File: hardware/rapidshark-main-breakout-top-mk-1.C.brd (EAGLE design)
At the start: 44 x 18 mm, 14 parts, among them U1 ADAFRUIT_METRO_MINIBIGHOLES

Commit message: asdlkfjaklsdfjsdlk
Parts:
- added JP1: M03JST-PTH-VERT, a_parts:JST-3-PH-VERT-PTH
- ACCEL, PUSHER: device A_butts:JST-6-PH-VERT-PTH -> a_parts:JST-6-PH-VERT-PTH
- BUTT, CLIP, DISP, TRIG: device A_butts:JST-4-PH-VERT-PTH -> a_parts:JST-4-PH-VERT-PTH
- F1: device A_butts:PTC-1206 -> a_parts:PTC-1206
- FRAME1: device A_butts:DUMMY -> a_parts:DUMMY
- R1, R2: device A_butts:R0805 -> a_parts:R0603-TIGHTER
- TVS: device A_butts:SMA-DIODE-TVS-BIDIR -> a_parts:SMA-DIODE-TVS-BIDIR
- U$2: device A_butts:COW_SMALL -> a_parts:COW_SMALL
- U$3: device A_butts:OSHWLOGO_TINY_SILKONLY -> a_parts:OSHWLOGO_TINY_SILKONLY
- U1: device A_butts:ADAFRUIT_METRO_MINI_BIGHOLES -> a_parts:ADAFRUIT_METRO_MINI_BIGHOLES
- moved R1 1.00 mm to (38.0, 11.0)
- moved R2 1.00 mm to (38.0, 7.00)
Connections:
- removed net ACCEL_A: ACCEL.1, U1.9
- removed net ACCEL_B: ACCEL.3, U1.11
- new net N$2: U1.9
- new net N$3: U1.11
- new net N$4: U1.14
- net 5V: now also ACCEL.5, DISP.2; no longer ACCEL.4, DISP.1
- net GND: now also ACCEL.6, DISP.1; no longer ACCEL.5, DISP.2, U1.26
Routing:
- net 5V: track 70.0 -> 65.1 mm
- net ACCEL_B: track 4.89 -> 0.00 mm
- net ACCEL_A: track 4.80 -> 0.00 mm
- net SDA: track 15.2 -> 13.9 mm

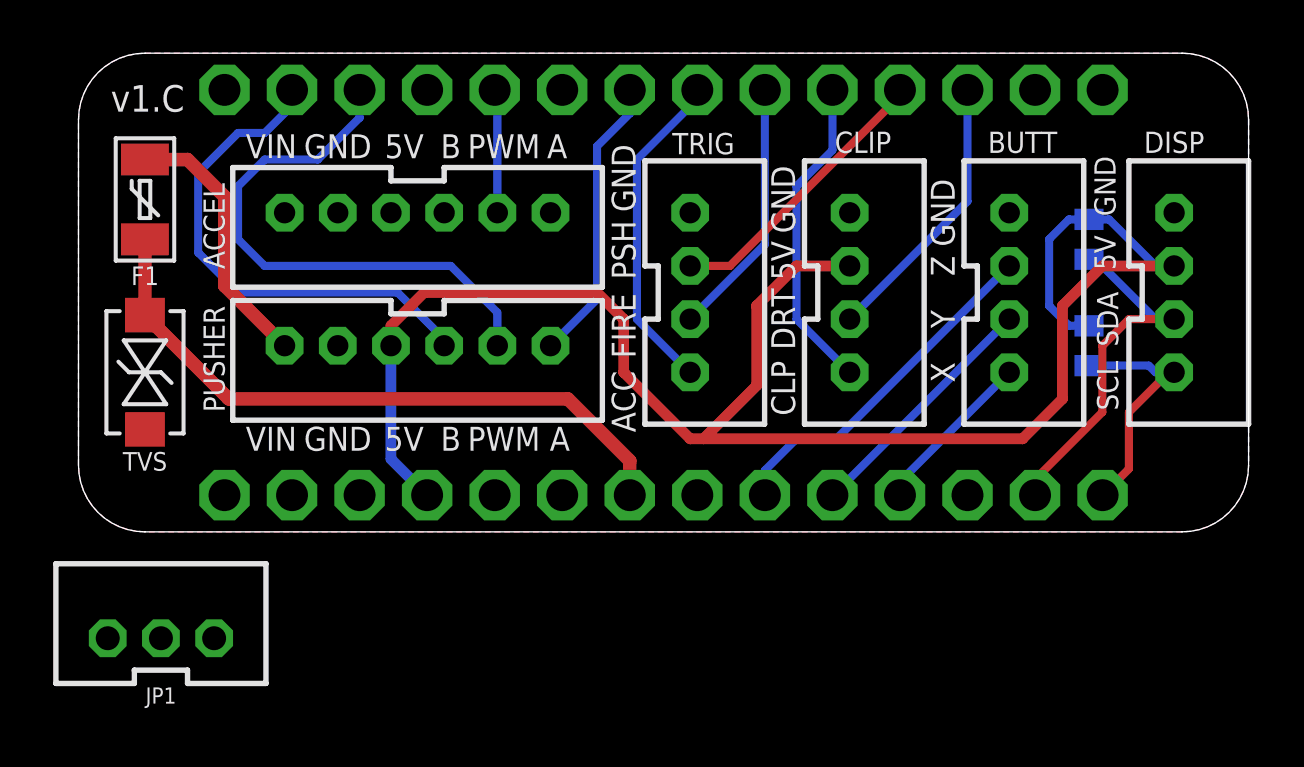
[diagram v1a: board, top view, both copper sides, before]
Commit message: new connector board for new motor driver and lipo sensor
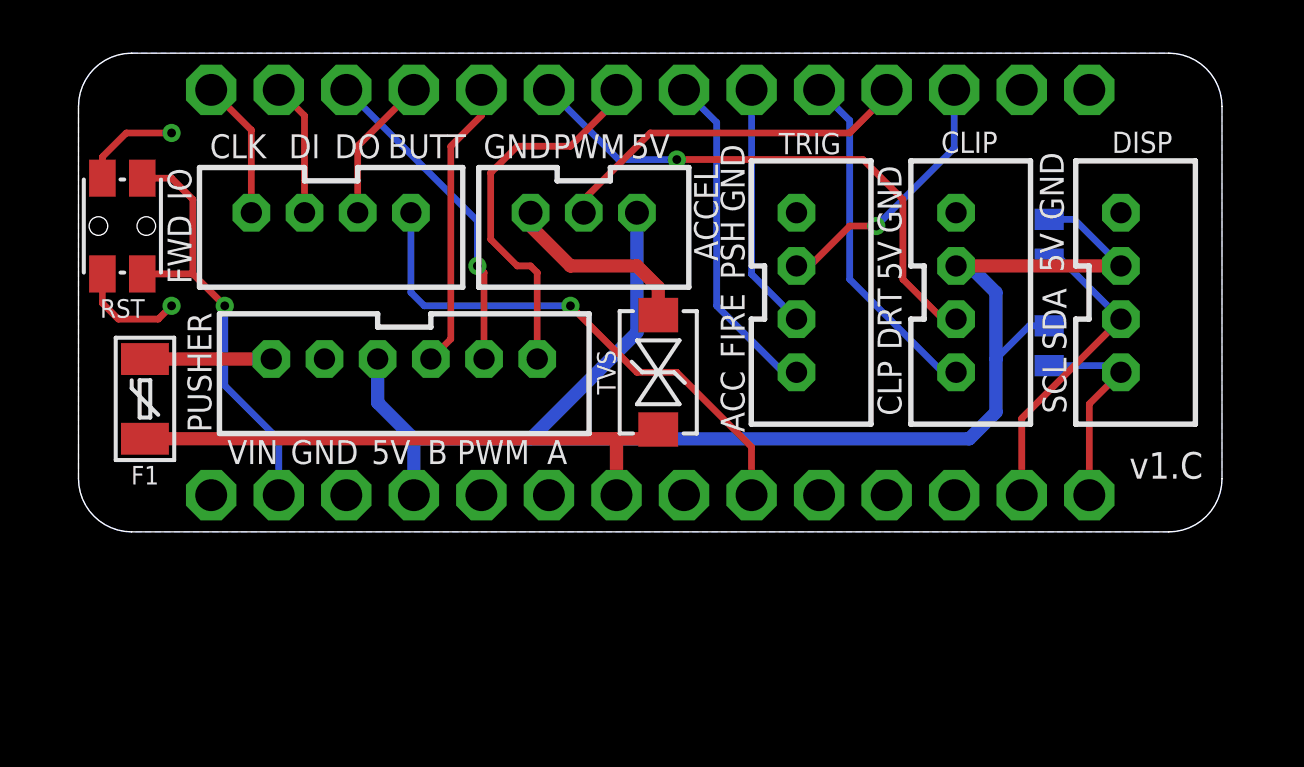
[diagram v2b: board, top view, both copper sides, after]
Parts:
- removed BUTT: M04JST-PTH-VERT, a_parts:JST-4-PH-VERT-PTH
- removed JP1: M03JST-PTH-VERT, a_parts:JST-3-PH-VERT-PTH
- removed U$3: (no value), a_parts:OSHWLOGO_TINY_SILKONLY
- added FWD_IO: M04JST-PTH-VERT, a_parts:JST-4-PH-VERT-PTH
- added RST: SPST-NO-TACTCK-PTS840-GK, a_parts:TACTILE-SMD-CK-PTS840-GK
- ACCEL: value M06JST-PH-PTH-VERT -> M03JST-PTH-VERT-CENTERED; device a_parts:JST-6-PH-VERT-PTH -> a_parts:JST-3-PH-VERT-PTH-CENTERED
- TVS: value (none) -> 15V
- moved TVS 19.3 mm to (21.8, 6.00), turned to 270 degrees
- moved F1 7.50 mm to (2.50, 5.00)
- moved ACCEL 6.25 mm to (19.0, 12.0)
- moved CLIP 4.00 mm to (33.0, 12.0)
- moved TRIG 4.00 mm to (27.0, 12.0)
- moved DISP 2.00 mm to (39.2, 12.0)
- moved R1 1.50 mm to (36.5, 11.0)
- moved R2 1.50 mm to (36.5, 7.00)
- moved U$2 1.00 mm to (4.50, 8.50)
- moved PUSHER 0.71 mm to (12.2, 6.50)
- moved U1 0.50 mm to (21.5, 9.00)
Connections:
- removed net N$2: U1.9
- removed net N$3: U1.11
- removed net N$4: U1.14
- removed net X: BUTT.4, U1.25
- removed net Y: BUTT.3, U1.24
- removed net Z: BUTT.2, U1.23
- new net BMON_CLK: FWD_IO.4, U1.14
- new net BMON_MISO: FWD_IO.3, U1.13
- new net BMON_MOSI: FWD_IO.2, U1.11
- new net BUTT: FWD_IO.1, U1.23
- new net RESET: RST.1, RST.2, U1.16
- net 5V: now also ACCEL.1; no longer ACCEL.5
- net ACCEL_PWM: now also U1.4; no longer U1.10
- net DART: now also U1.9; no longer U1.3
- net GND: now also ACCEL.3, RST.3, RST.4; no longer ACCEL.6, BUTT.1
- net PUSH: now also U1.3; no longer U1.4
- net PUSH_B: now also U1.10; no longer U1.13
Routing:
- net BUTT: track 0.00 -> 20.0 mm, vias 0 -> 1
- net RESET: track 0.00 -> 16.6 mm, vias 0 -> 1
- net GND: track 0.00 -> 15.2 mm, vias 0 -> 2
- net Z: track 13.3 -> 0.00 mm
- net DART: track 10.5 -> 20.6 mm, vias 0 -> 1
- net Y: track 9.39 -> 0.00 mm
- net ACCEL_PWM: track 4.66 -> 13.7 mm
- net PUSH_PWM: track 20.8 -> 12.3 mm, vias 0 -> 1
- net 5V: track 65.1 -> 56.7 mm
- net PUSH_B: track 19.0 -> 10.9 mm
- net X: track 6.32 -> 0.00 mm
- net BMON_MOSI: track 0.00 -> 5.49 mm
- net VIN: track 10.1 -> 4.75 mm
- net BMON_CLK: track 0.00 -> 5.25 mm
- net BMON_MISO: track 0.00 -> 5.02 mm
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- removed copper zone on layer 1, net GND
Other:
- board size 44 x 18 mm -> 43 x 18 mm
- board text added: "BUTT"
- board text added: "CLK"
- board text added: "DI"
- board text added: "DO"
- board text removed: "X"
- board text removed: "Y"
- board text removed: "Z"
